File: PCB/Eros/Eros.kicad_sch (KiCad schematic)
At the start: 113 parts, among them IC1 ADS1292RIPBS, J1 USB_C_PowerOnly_6P, J2 UART, J3 Li-ion, J4 Conn_01x08_Socket, J5 AudioJack3, J6 Micro_SD_Card, J7 Conn_01x03_Socket, Q1 BC817, SW1 SW_Push, SW2 SW_Push, SW4 SW_Push, SW5 SW_Push, SW6 SW_SPDT, U1 ESP32-WROOM-32E, U2 LIS3DH, U3 MCP73831-2-OT, U4 AP2112K-3.3, U6 MCP100-315D

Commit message: Sprawdzenie schematu i połączeń
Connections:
- net GND: now also SW2.1, SW2.SH; no longer SW2.2
- net RESET: now also SW2.2; no longer SW2.1
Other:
- moved on the sheet: SW2
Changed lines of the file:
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@@
 	(text "SPI SCREEN"
 		(exclude_from_sim no)
-		(at 345.186 196.85 0)
+		(at 345.186 198.374 0)
 		(effects
 			(font
@@
 	(text "POWER SECTION"
 		(exclude_from_sim no)
-		(at 115.824 223.266 0)
+		(at 115.57 218.694 0)
 		(effects
 			(font
@@
 		)
 		(property "Value" "+3.3V"
-			(at 180.086 246.634 0)
+			(at 181.864 245.872 0)
 			(effects
 				(font
@@
 		(on_board yes)
 		(dnp no)
-		(fields_autoplaced yes)
 		(property "Reference" "#PWR028"
 			(at 68.58 257.81 0)
@@
 		)
 		(property "Value" "GND"
-			(at 68.58 256.54 0)
+			(at 68.58 255.524 0)
 			(effects
 				(font
@@
 	(symbol
 		(lib_id "Moje_symbole:SW_Push")
-		(at 58.42 163.83 90)
+		(at 58.42 163.83 270)
 		(mirror x)
 		(unit 1)
@@
 		(dnp no)
 		(property "Reference" "SW2"
-			(at 54.102 160.02 90)
+			(at 62.738 167.64 90)
 			(effects
 				(font
@@
 		)
 		(property "Value" "SW_Push"
-			(at 60.198 168.656 0)
+			(at 56.642 159.004 0)
 			(effects
 				(font
@@
 		)
 		(property "Footprint" "Button_Switch_SMD:SW_Push_1P1T-SH_NO_CK_KMR2xxG"
-			(at 53.34 163.83 0)
+			(at 63.5 163.83 0)
 			(effects
 				(font
@@
 		)
 		(property "Datasheet" "~"
-			(at 53.34 163.83 0)
+			(at 63.5 163.83 0)
 			(effects
 				(font

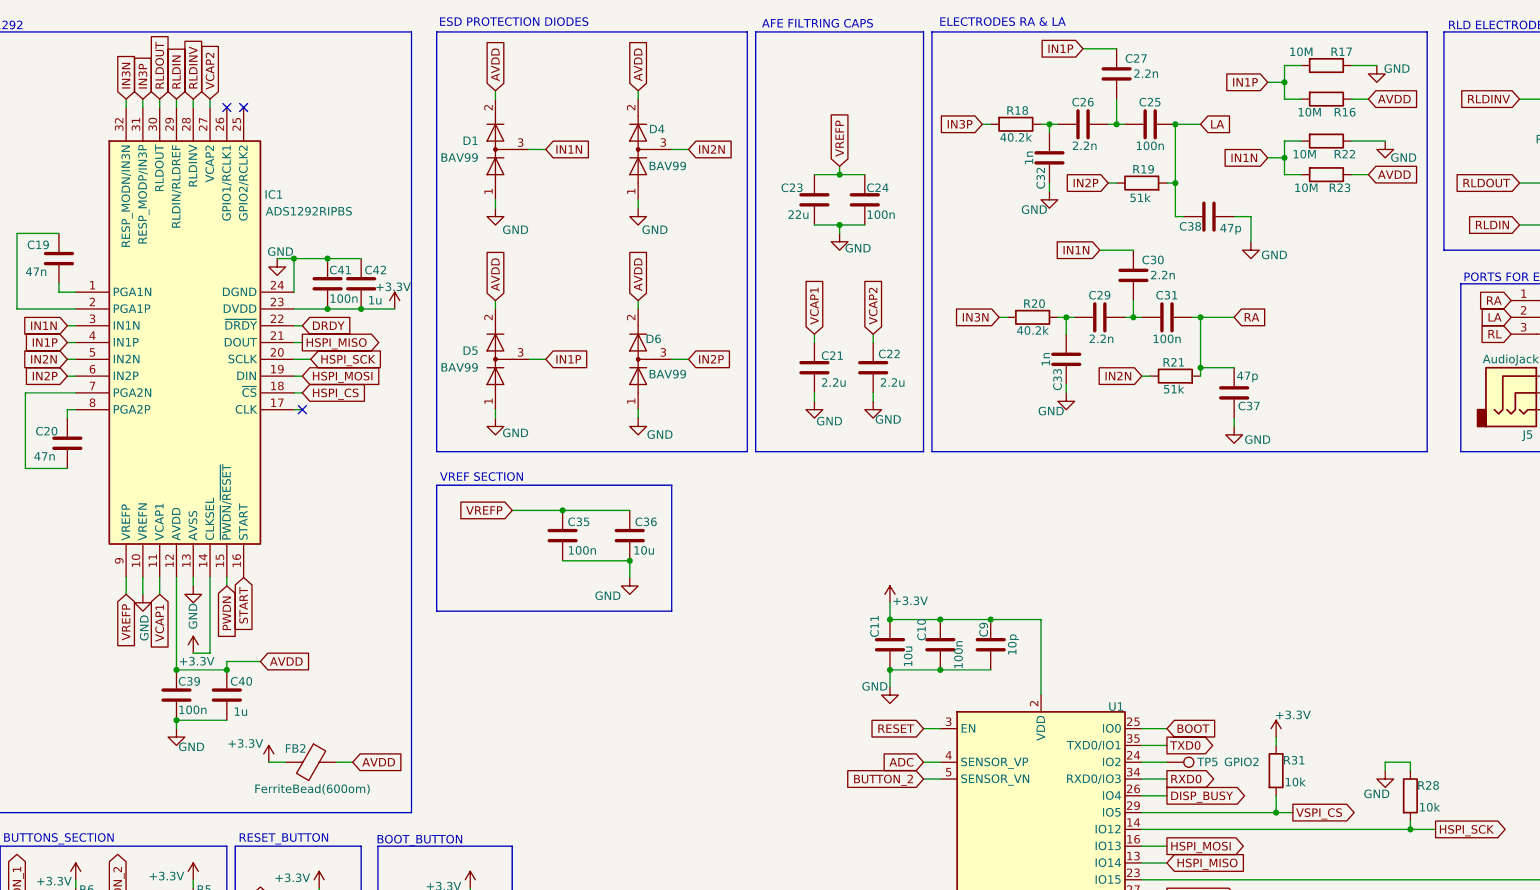
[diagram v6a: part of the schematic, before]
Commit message: Add A GND
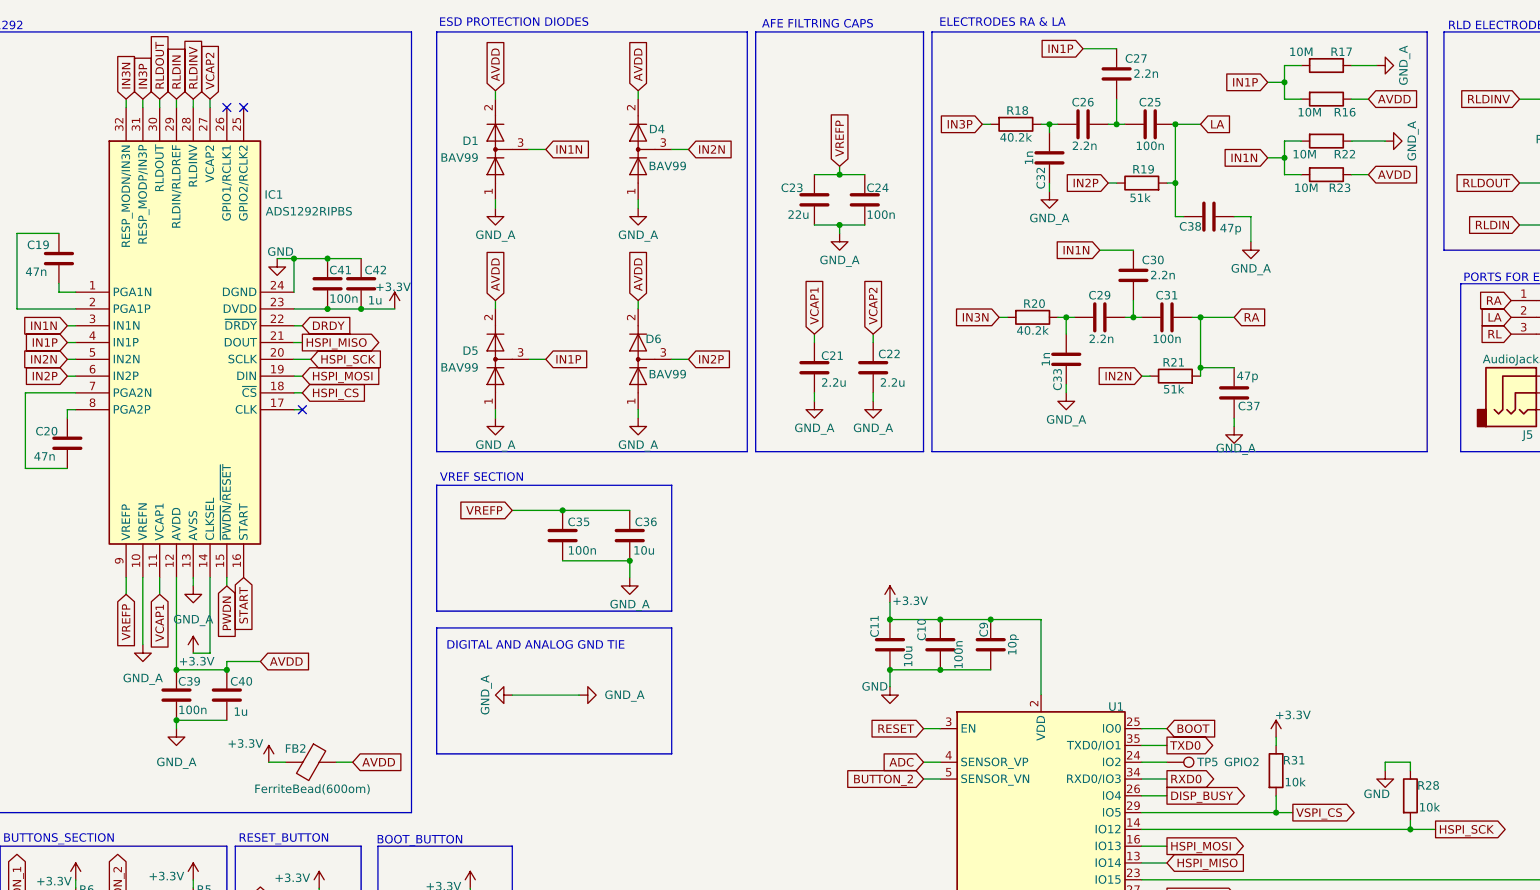
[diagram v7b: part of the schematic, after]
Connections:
- net GND: no longer C21.2, C22.2, C23.2, C24.2, C32.2, C33.2, C35.2, C36.2, C37.1, C38.2, C39.2, C40.2, D1.1 (K), D4.1 (K), D5.1 (K), D6.1 (K), IC1.10 (VREFN), IC1.13 (AVSS), R17.1, R22.1
- new net GND_A: C21.2, C22.2, C23.2, C24.2, C32.2, C33.2, C35.2, C36.2, C37.1, C38.2, C39.2, C40.2, D1.1 (K), D4.1 (K), D5.1 (K), D6.1 (K), IC1.10 (VREFN), IC1.13 (AVSS), R17.1, R22.1
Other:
- note added: "DIGITAL AND ANALOG GND TIE"

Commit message: add nettie
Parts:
- added NT1: NetTie_2, NetTie:NetTie-2_SMD_Pad0.5mm, symbol Device:NetTie_2
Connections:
- net GND: now also NT1.2
- net GND_A: now also NT1.1
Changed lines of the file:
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@@
 	(wire
 		(pts
+			(xy 96.52 116.84) (xy 99.06 116.84)
+		)
+		(stroke
+			(width 0)
+			(type default)
+		)
+	)
+	(wire
+		(pts
 			(xy 187.96 30.48) (xy 189.23 30.48)
 		)
@@
 	(wire
 		(pts
-			(xy 96.52 116.84) (xy 106.68 116.84)
-		)
-		(stroke
-			(width 0)
-			(type default)
-		)
-	)
-	(wire
-		(pts
 			(xy 40.64 99.06) (xy 40.64 109.22)
 		)
@@
 	(wire
 		(pts
+			(xy 104.14 116.84) (xy 106.68 116.84)
+		)
+		(stroke
+			(width 0)
+			(type default)
+		)
+	)
+	(wire
+		(pts
 			(xy 21.59 171.45) (xy 26.67 171.45)
 		)
@@
 	)
 	(symbol
+		(lib_id "power:GND")
+		(at 106.68 116.84 90)
+		(unit 1)
+		(exclude_from_sim no)
+		(in_bom yes)
+		(on_board yes)
+		(dnp no)
+		(property "Reference" "#PWR075"
+			(at 113.03 116.84 0)
+			(effects
+				(font
+					(size 1.27 1.27)
+				)
+				(hide yes)
+			)
+		)
+		(property "Value" "GND"
+			(at 110.744 116.84 0)
+			(effects
+				(font
+					(size 1.27 1.27)
+				)
+			)
+		)
+		(property "Footprint" ""
+			(at 106.68 116.84 0)
+			(effects
+				(font
+					(size 1.27 1.27)
+				)
+				(hide yes)
+			)
+		)
+		(property "Datasheet" ""
+			(at 106.68 116.84 0)
+			(effects
+				(font
+					(size 1.27 1.27)
+				)
+				(hide yes)
+			)
+		)
+		(property "Description" "Power symbol creates a global label with name \"GND\" , ground"
+			(at 106.68 116.84 0)
+			(effects
+				(font
+					(size 1.27 1.27)
+				)
+				(hide yes)
+			)
+		)
+		(pin "1"
+		)
+		(instances
+			(project "Eros"
+				(path "/0de1f6b5-5206-4036-b96d-057d224718dc"
+					(reference "#PWR075")
+					(unit 1)
+				)
+			)
+		)
+	)
+	(symbol
 		(lib_id "Device:C")
 		(at 53.34 116.84 0)
@@
 	)
 	(symbol
+		(lib_id "Device:NetTie_2")
+		(at 101.6 116.84 0)
+		(unit 1)
+		(exclude_from_sim no)
+		(in_bom no)
+		(on_board yes)
+		(dnp no)
+		(fields_autoplaced yes)
+		(property "Reference" "NT1"
+			(at 101.6 111.76 0)
+			(effects
+				(font
+					(size 1.27 1.27)
+				)
+			)
+		)
+		(property "Value" "NetTie_2"
+			(at 101.6 114.3 0)
+			(effects
+				(font
+					(size 1.27 1.27)
+				)
+			)
+		)
+		(property "Footprint" "NetTie:NetTie-2_SMD_Pad0.5mm"
+			(at 101.6 116.84 0)
+			(effects
+				(font
+					(size 1.27 1.27)
+				)
+				(hide yes)
+			)
+		)
+		(property "Datasheet" "~"
+			(at 101.6 116.84 0)
+			(effects
+				(font
+					(size 1.27 1.27)
+				)
+				(hide yes)
+			)
+		)
+		(property "Description" "Net tie, 2 pins"
+			(at 101.6 116.84 0)
+			(effects
+				(font
+					(size 1.27 1.27)
+				)
+				(hide yes)
+			)
+		)
+		(pin "2"
+		)
+		(pin "1"
+		)
+		(instances
+			(project "Eros"
+				(path "/0de1f6b5-5206-4036-b96d-057d224718dc"
+					(reference "NT1")
+					(unit 1)
+				)
+			)
+		)
+	)
+	(symbol
 		(lib_id "power:GND1")
 		(at 96.52 116.84 270)
@@
 					(unit 1)
 				)
-			)
-		)
-	)
-	(symbol
-		(lib_id "power:GND1")
-		(at 106.68 116.84 90)
-		(unit 1)
-		(exclude_from_sim no)
-		(in_bom yes)
-		(on_board yes)
-		(dnp no)
-		(fields_autoplaced yes)
-		(property "Reference" "#PWR075"
-			(at 113.03 116.84 0)
-			(effects
-				(font
-					(size 1.27 1.27)
-				)
-				(hide yes)
-			)
-		)
-		(property "Value" "GND_A"
-			(at 110.49 116.8399 90)
-			(effects
-				(font
-					(size 1.27 1.27)
-				)
-				(justify right)
-			)
-		)
-		(property "Footprint" ""
-			(at 106.68 116.84 0)
-			(effects
-				(font
-					(size 1.27 1.27)
-				)
-				(hide yes)
-			)
-		)
-		(property "Datasheet" ""
-			(at 106.68 116.84 0)
-			(effects
-				(font
-					(size 1.27 1.27)
-				)
-				(hide yes)
-			)
-		)
-		(property "Description" "Power symbol creates a global label with name \"GND1\" , ground"
-			(at 106.68 116.84 0)
-			(effects
-				(font
-					(size 1.27 1.27)
-				)
-				(hide yes)
-			)
-		)
-		(pin "1"
-		)
-		(instances
-			(project "Eros"
-				(path "/0de1f6b5-5206-4036-b96d-057d224718dc"
-					(reference "#PWR075")
-					(unit 1)
-				)
